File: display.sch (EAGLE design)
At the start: 9 parts

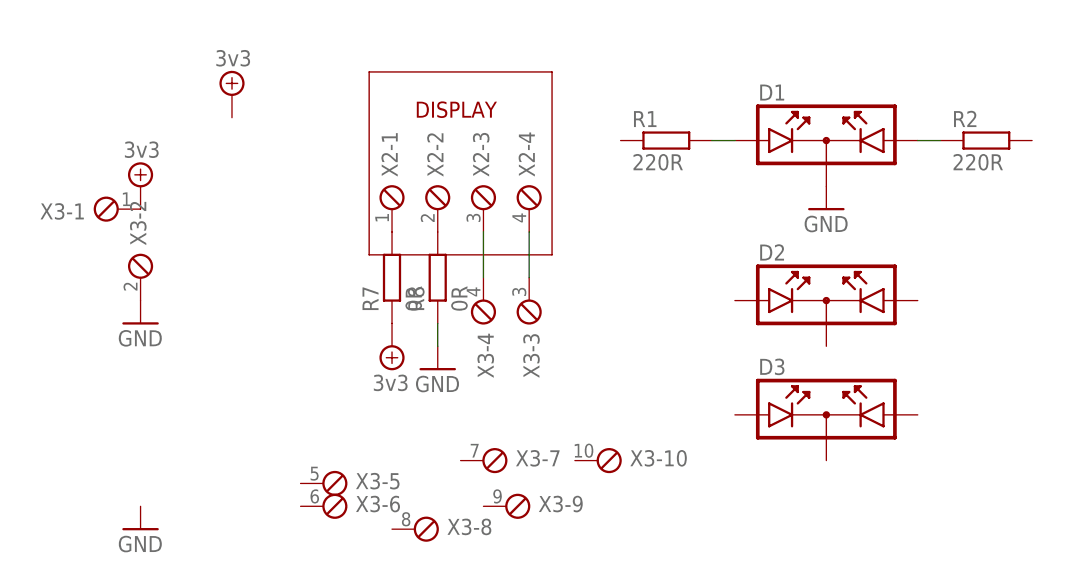
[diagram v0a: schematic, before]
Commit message: front panel board made to fit
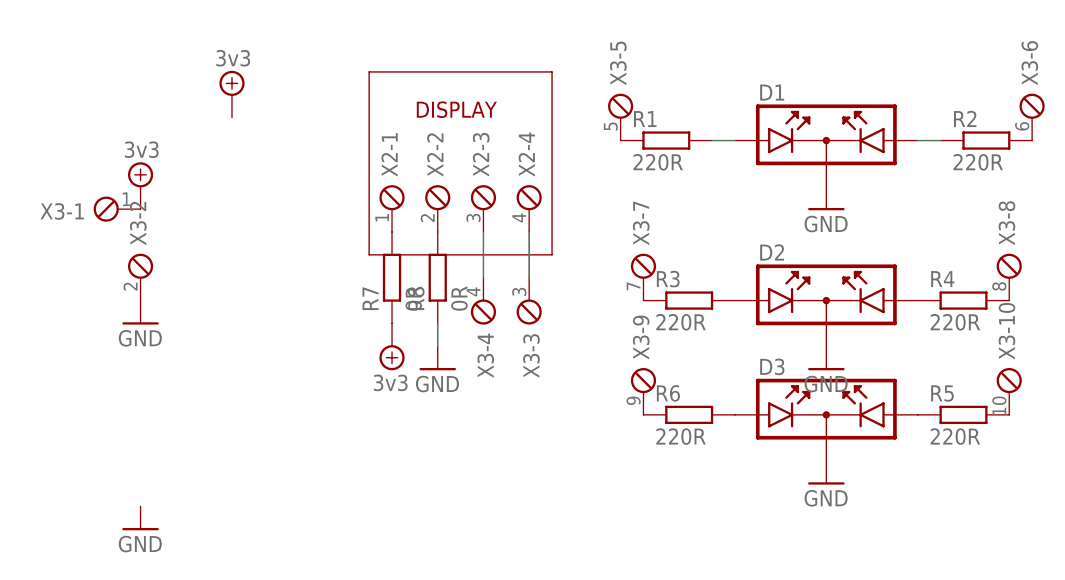
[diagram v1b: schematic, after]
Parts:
- added R3, R4, R5, R6: 220R, rcl:R-EU_R0603
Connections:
- new net N$10: D3.A1, R6.2
- new net N$11: R3.1, X3-7.1
- new net N$12: R4.2, X3-8.1
- new net N$13: R6.1, X3-9.1
- new net N$14: R5.2, X3-10.1
- new net N$5: R1.1, X3-5.1
- new net N$6: R2.2, X3-6.1
- new net N$7: D2.A1, R3.2
- new net N$8: D2.A2, R4.1
- new net N$9: D3.A2, R5.1
- net GND: now also D2.K, D3.K
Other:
- moved on the sheet: X3-10, X3-5, X3-6, X3-7, X3-8, X3-9
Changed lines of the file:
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@@
 <part name="D2" library="special" deviceset="DUOLED" device=""/>
 <part name="D3" library="special" deviceset="DUOLED" device=""/>
+<part name="R3" library="rcl" deviceset="R-EU_" device="R0603" value="220R"/>
+<part name="R4" library="rcl" deviceset="R-EU_" device="R0603" value="220R"/>
+<part name="R5" library="rcl" deviceset="R-EU_" device="R0603" value="220R"/>
+<part name="R6" library="rcl" deviceset="R-EU_" device="R0603" value="220R"/>
+<part name="GND5" library="supply1" deviceset="GND" device=""/>
+<part name="GND6" library="supply1" deviceset="GND" device=""/>
 </parts>
 <sheets>
@@
 <instance part="X3" gate="-1" x="43.18" y="78.74" rot="R180"/>
 <instance part="X3" gate="-2" x="45.72" y="71.12" rot="R90"/>
-<instance part="X3" gate="-5" x="66.04" y="48.26"/>
-<instance part="X3" gate="-6" x="66.04" y="45.72"/>
-<instance part="X3" gate="-9" x="86.36" y="45.72"/>
-<instance part="X3" gate="-10" x="96.52" y="50.8"/>
+<instance part="X3" gate="-5" x="99.06" y="88.9" rot="R90"/>
+<instance part="X3" gate="-6" x="144.78" y="88.9" rot="R90"/>
+<instance part="X3" gate="-9" x="101.6" y="58.42" rot="R90"/>
+<instance part="X3" gate="-10" x="142.24" y="58.42" rot="R90"/>
 <instance part="R7" gate="G$1" x="73.66" y="71.12" rot="R90"/>
 <instance part="R8" gate="G$1" x="78.74" y="71.12" rot="R90"/>
 <instance part="X3" gate="-3" x="88.9" y="68.58" rot="R270"/>
 <instance part="X3" gate="-4" x="83.82" y="68.58" rot="R270"/>
-<instance part="X3" gate="-7" x="83.82" y="50.8"/>
-<instance part="X3" gate="-8" x="76.2" y="43.18"/>
+<instance part="X3" gate="-7" x="101.6" y="71.12" rot="R90"/>
+<instance part="X3" gate="-8" x="142.24" y="71.12" rot="R90"/>
 <instance part="GND3" gate="1" x="121.92" y="78.74"/>
 <instance part="D2" gate="G$1" x="121.92" y="68.58"/>
 <instance part="D3" gate="G$1" x="121.92" y="55.88"/>
+<instance part="R3" gate="G$1" x="106.68" y="68.58"/>
+<instance part="R4" gate="G$1" x="137.16" y="68.58"/>
+<instance part="R5" gate="G$1" x="137.16" y="55.88"/>
+<instance part="R6" gate="G$1" x="106.68" y="55.88"/>
+<instance part="GND5" gate="1" x="121.92" y="60.96"/>
+<instance part="GND6" gate="1" x="121.92" y="48.26"/>
 </instances>
 <busses>
@@
 <pinref part="GND3" gate="1" pin="GND"/>
 </segment>
+<segment>
+<pinref part="D2" gate="G$1" pin="K"/>
+<pinref part="GND5" gate="1" pin="GND"/>
+</segment>
+<segment>
+<pinref part="D3" gate="G$1" pin="K"/>
+<pinref part="GND6" gate="1" pin="GND"/>
+</segment>
 </net>
 <net name="N$15" class="0">
@@
 </segment>
 </net>
+<net name="N$5" class="0">
+<segment>
+<pinref part="R1" gate="G$1" pin="1"/>
+<pinref part="X3" gate="-5" pin="1"/>
+</segment>
+</net>
+<net name="N$6" class="0">
+<segment>
+<pinref part="R2" gate="G$1" pin="2"/>
+<pinref part="X3" gate="-6" pin="1"/>
+</segment>
+</net>
+<net name="N$7" class="0">
+<segment>
+<pinref part="D2" gate="G$1" pin="A1"/>
+<pinref part="R3" gate="G$1" pin="2"/>
+</segment>
+</net>
+<net name="N$8" class="0">
+<segment>
+<pinref part="D2" gate="G$1" pin="A2"/>
+<pinref part="R4" gate="G$1" pin="1"/>
+</segment>
+</net>
+<net name="N$9" class="0">
+<segment>
+<pinref part="D3" gate="G$1" pin="A2"/>
+<pinref part="R5" gate="G$1" pin="1"/>
+</segment>
+</net>
+<net name="N$10" class="0">
+<segment>
+<pinref part="D3" gate="G$1" pin="A1"/>
+<pinref part="R6" gate="G$1" pin="2"/>
+</segment>
+</net>
+<net name="N$11" class="0">
+<segment>
+<pinref part="R3" gate="G$1" pin="1"/>
+<pinref part="X3" gate="-7" pin="1"/>
+</segment>
+</net>
+<net name="N$12" class="0">
+<segment>
+<pinref part="R4" gate="G$1" pin="2"/>
+<pinref part="X3" gate="-8" pin="1"/>
+</segment>
+</net>
+<net name="N$13" class="0">
+<segment>
+<pinref part="R6" gate="G$1" pin="1"/>
+<pinref part="X3" gate="-9" pin="1"/>
+</segment>
+</net>
+<net name="N$14" class="0">
+<segment>
+<pinref part="R5" gate="G$1" pin="2"/>
+<pinref part="X3" gate="-10" pin="1"/>
+</segment>
+</net>
